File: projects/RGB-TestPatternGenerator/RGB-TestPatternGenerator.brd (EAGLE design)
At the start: 100 x 80 mm, 47 parts, among them IC1 7805TV, IC2 7809TV, IC3 4060N, IC4 4040N, IC5 74HC10N, IC6 4082N, IC7 74HC32N, IC8 74LS157N, X1 D-SUB15-HDR15RA, X2 PWR, Y1 8MHz

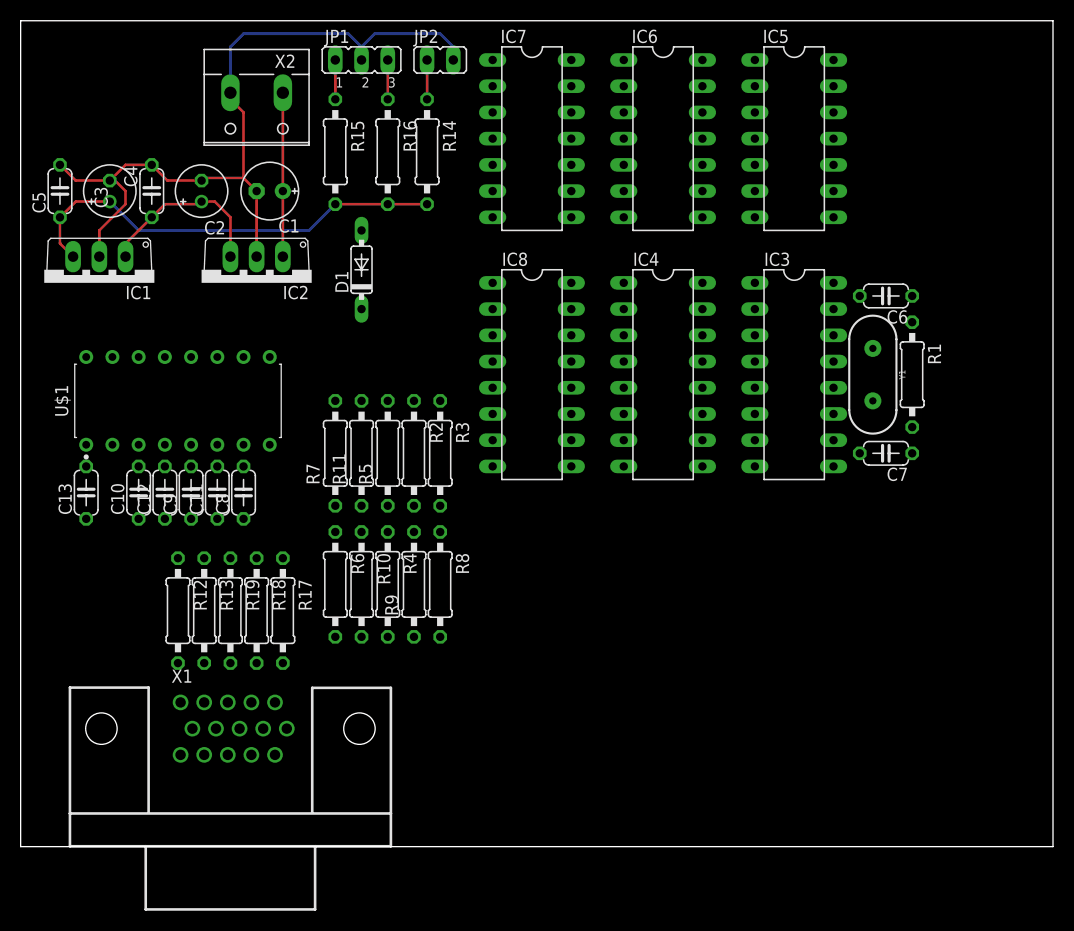
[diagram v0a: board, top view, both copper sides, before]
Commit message: fix: layout fixed and cam data added
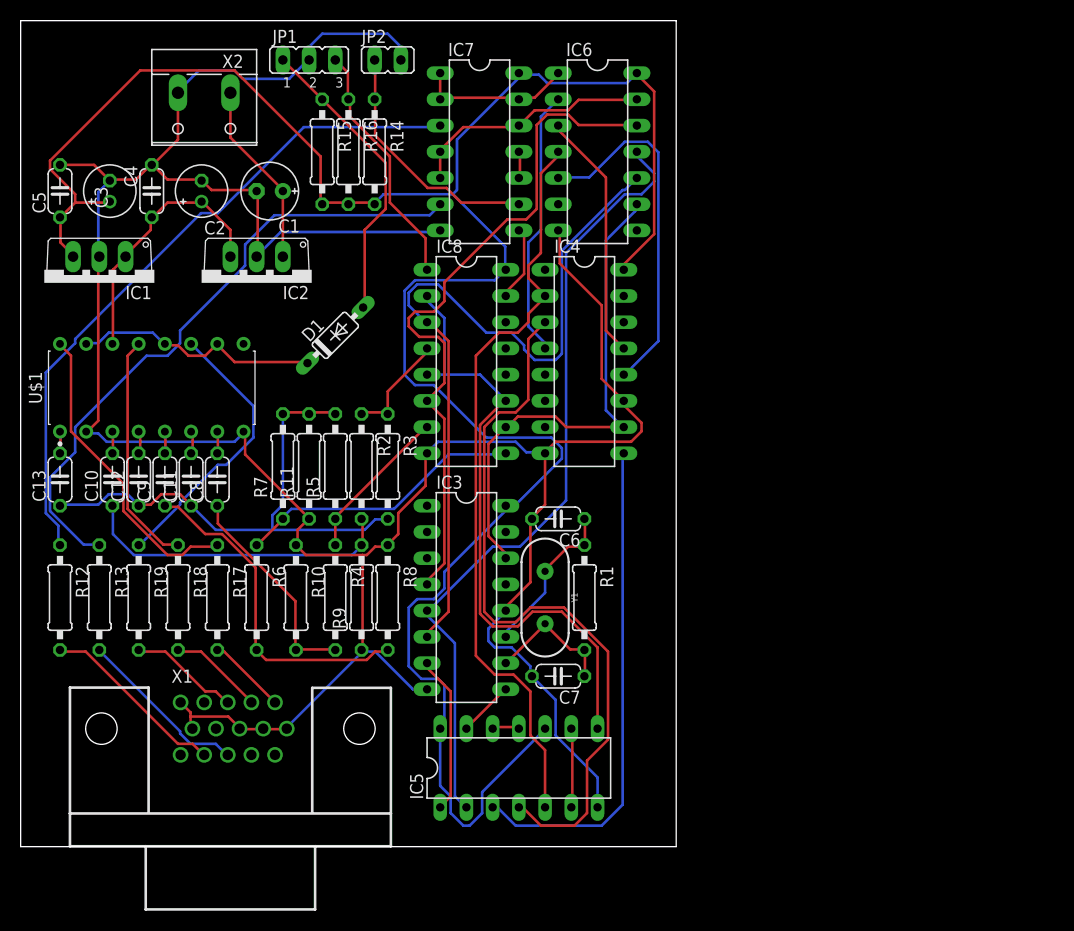
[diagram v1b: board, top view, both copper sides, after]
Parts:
- moved IC5 66.5 mm to (48.3, 7.62), turned to 0 degrees
- moved IC3 38.4 mm to (43.2, 24.1)
- moved R1 38.4 mm to (54.6, 24.1)
- moved Y1 38.4 mm to (50.8, 24.1)
- moved C6 38.4 mm to (52.1, 31.8)
- moved C7 38.4 mm to (52.1, 16.5)
- moved R12 11.5 mm to (3.81, 24.1)
- moved R13 10.2 mm to (7.62, 24.1)
- moved R19 8.98 mm to (11.4, 24.1)
- moved R6 7.73 mm to (22.9, 24.1)
- moved IC4 7.73 mm to (54.6, 47.0)
- moved R18 7.73 mm to (15.2, 24.1)
- moved D1 6.84 mm to (30.5, 49.5), turned to 45 degrees
- moved IC8 6.48 mm to (43.2, 47.0)
- moved R10 6.48 mm to (26.7, 24.1)
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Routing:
- net GND: track 77.2 -> 286.0 mm
- net +5V: track 42.7 -> 220.9 mm
- net N$4: track 0.00 -> 77.5 mm
- net N$8: track 0.00 -> 74.9 mm
- net N$12: track 0.00 -> 73.1 mm
- net N$13: track 0.00 -> 70.6 mm
- net N$5: track 0.00 -> 66.9 mm
- net N$31: track 0.00 -> 65.8 mm
- net N$30: track 0.00 -> 61.5 mm
- net N$10: track 0.00 -> 60.6 mm
- net N$25: track 0.00 -> 52.3 mm
- net N$9: track 0.00 -> 50.0 mm
- net N$14: track 0.00 -> 48.3 mm
- net N$18: track 0.00 -> 34.6 mm
- net N$26: track 0.00 -> 32.9 mm
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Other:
- board size 100 x 80 mm -> 63.5 x 80 mm
